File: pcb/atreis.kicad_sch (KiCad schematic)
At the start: 114 parts, among them SW1 SW_Push, U1 Elite-C

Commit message: Completed tracks and edge. Cleaned up drawings.
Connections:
- net ROW5: now also U1.17 (A0/PF7); no longer U1.13 (10/PB6)
- net ROW6: now also U1.16 (15/PB1); no longer U1.14 (16/PB2)
- net ROW8: now also U1.14 (16/PB2); no longer U1.16 (15/PB1)
- net ROW9: now also U1.13 (10/PB6); no longer U1.17 (A0/PF7)
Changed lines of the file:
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@@
     )
   )
-  (global_label "ROW5" (shape input) (at 111.76 170.18 0) (fields_autoplaced)
+  (global_label "ROW5" (shape input) (at 111.76 160.02 0) (fields_autoplaced)
     (effects (font (size 1.27 1.27)) (justify left))
-    (property "Intersheet References" "${INTERSHEET_REFS}" (id 0) (at -57.15 3.81 0)
+    (property "Intersheet References" "${INTERSHEET_REFS}" (id 0) (at -57.15 -6.35 0)
       (effects (font (size 1.27 1.27)) hide)
     )
@@
     )
   )
-  (global_label "ROW8" (shape input) (at 111.76 162.56 0) (fields_autoplaced)
+  (global_label "ROW8" (shape input) (at 111.76 167.64 0) (fields_autoplaced)
     (effects (font (size 1.27 1.27)) (justify left))
-    (property "Intersheet References" "${INTERSHEET_REFS}" (id 0) (at -57.15 -11.43 0)
+    (property "Intersheet References" "${INTERSHEET_REFS}" (id 0) (at -57.15 -6.35 0)
       (effects (font (size 1.27 1.27)) hide)
     )
@@
     )
   )
-  (global_label "ROW9" (shape input) (at 111.76 160.02 0) (fields_autoplaced)
+  (global_label "ROW9" (shape input) (at 111.76 170.18 0) (fields_autoplaced)
     (effects (font (size 1.27 1.27)) (justify left))
-    (property "Intersheet References" "${INTERSHEET_REFS}" (id 0) (at -57.15 -16.51 0)
+    (property "Intersheet References" "${INTERSHEET_REFS}" (id 0) (at -57.15 -6.35 0)
       (effects (font (size 1.27 1.27)) hide)
     )
@@
     )
   )
-  (global_label "ROW6" (shape input) (at 111.76 167.64 0) (fields_autoplaced)
+  (global_label "ROW6" (shape input) (at 111.76 162.56 0) (fields_autoplaced)
     (effects (font (size 1.27 1.27)) (justify left))
-    (property "Intersheet References" "${INTERSHEET_REFS}" (id 0) (at -57.15 -1.27 0)
+    (property "Intersheet References" "${INTERSHEET_REFS}" (id 0) (at -57.15 -6.35 0)
       (effects (font (size 1.27 1.27)) hide)
     )

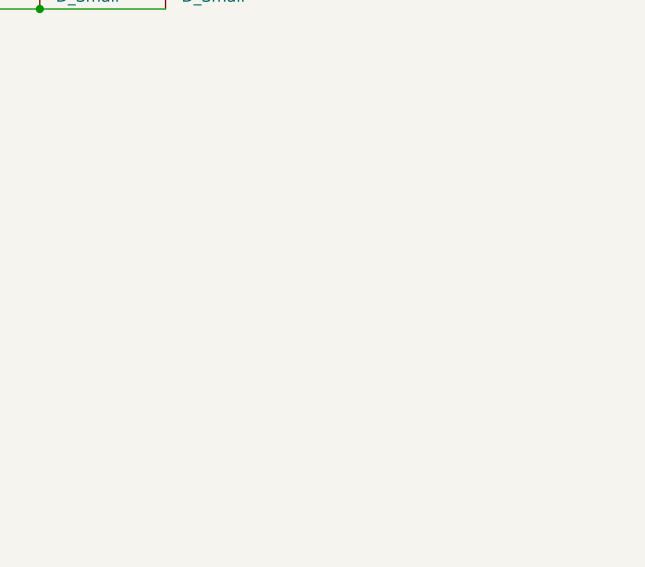
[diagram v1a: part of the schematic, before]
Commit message: Rerouted some of the tracks. Much nicer now. Rerouted tracks to make the holes thru holes, to use with spacers. Re-generated gerber file.
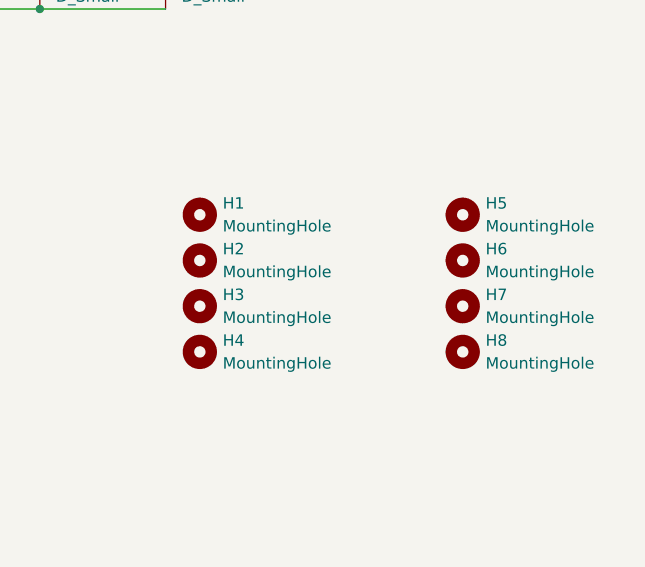
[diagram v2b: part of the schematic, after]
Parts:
- added H1, H2, H3, H4, H5, H6, H7, H8: MountingHole, kbd:M2_Hole_TH_Outside, symbol Mechanical:MountingHole
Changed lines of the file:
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@@
     (pin "2")
+  )
+  (symbol (lib_id "Mechanical:MountingHole") (at 175.26 144.78 0) (unit 1)
+    (in_bom yes) (on_board yes) (fields_autoplaced)
+    (property "Reference" "H3" (id 0) (at 177.8 143.5099 0)
+      (effects (font (size 1.27 1.27)) (justify left))
+    )
+    (property "Value" "MountingHole" (id 1) (at 177.8 146.0499 0)
+      (effects (font (size 1.27 1.27)) (justify left))
+    )
+    (property "Footprint" "kbd:M2_Hole_TH_Outside" (id 2) (at 175.26 144.78 0)
+      (effects (font (size 1.27 1.27)) hide)
+    )
+    (property "Datasheet" "~" (id 3) (at 175.26 144.78 0)
+      (effects (font (size 1.27 1.27)) hide)
+    )
   )
   (symbol (lib_id "MX_Alps_Hybrid:MX-NoLED") (at 203.2 69.85 0) (unit 1)
@@
     (pin "1")
     (pin "2")
+  )
+  (symbol (lib_id "Mechanical:MountingHole") (at 204.47 134.62 0) (unit 1)
+    (in_bom yes) (on_board yes) (fields_autoplaced)
+    (property "Reference" "H5" (id 0) (at 207.01 133.3499 0)
+      (effects (font (size 1.27 1.27)) (justify left))
+    )
+    (property "Value" "MountingHole" (id 1) (at 207.01 135.8899 0)
+      (effects (font (size 1.27 1.27)) (justify left))
+    )
+    (property "Footprint" "kbd:M2_Hole_TH_Outside" (id 2) (at 204.47 134.62 0)
+      (effects (font (size 1.27 1.27)) hide)
+    )
+    (property "Datasheet" "~" (id 3) (at 204.47 134.62 0)
+      (effects (font (size 1.27 1.27)) hide)
+    )
   )
   (symbol (lib_id "MX_Alps_Hybrid:MX-NoLED") (at 203.2 53.34 0) (unit 1)
@@
     (pin "9")
   )
+  (symbol (lib_id "Mechanical:MountingHole") (at 204.47 149.86 0) (unit 1)
+    (in_bom yes) (on_board yes) (fields_autoplaced)
+    (property "Reference" "H8" (id 0) (at 207.01 148.5899 0)
+      (effects (font (size 1.27 1.27)) (justify left))
+    )
+    (property "Value" "MountingHole" (id 1) (at 207.01 151.1299 0)
+      (effects (font (size 1.27 1.27)) (justify left))
+    )
+    (property "Footprint" "kbd:M2_Hole_TH_Outside" (id 2) (at 204.47 149.86 0)
+      (effects (font (size 1.27 1.27)) hide)
+    )
+    (property "Datasheet" "~" (id 3) (at 204.47 149.86 0)
+      (effects (font (size 1.27 1.27)) hide)
+    )
+  )
   (symbol (lib_id "Device:D_Small") (at 185.42 92.71 90) (unit 1)
     (in_bom yes) (on_board yes)
@@
     (pin "1")
     (pin "2")
+  )
+  (symbol (lib_id "Mechanical:MountingHole") (at 175.26 149.86 0) (unit 1)
+    (in_bom yes) (on_board yes) (fields_autoplaced)
+    (property "Reference" "H4" (id 0) (at 177.8 148.5899 0)
+      (effects (font (size 1.27 1.27)) (justify left))
+    )
+    (property "Value" "MountingHole" (id 1) (at 177.8 151.1299 0)
+      (effects (font (size 1.27 1.27)) (justify left))
+    )
+    (property "Footprint" "kbd:M2_Hole_TH_Outside" (id 2) (at 175.26 149.86 0)
+      (effects (font (size 1.27 1.27)) hide)
+    )
+    (property "Datasheet" "~" (id 3) (at 175.26 149.86 0)
+      (effects (font (size 1.27 1.27)) hide)
+    )
   )
   (symbol (lib_id "MX_Alps_Hybrid:MX-NoLED") (at 147.32 69.85 0) (unit 1)
@@
     (pin "2")
   )
+  (symbol (lib_id "Mechanical:MountingHole") (at 204.47 139.7 0) (unit 1)
+    (in_bom yes) (on_board yes) (fields_autoplaced)
+    (property "Reference" "H6" (id 0) (at 207.01 138.4299 0)
+      (effects (font (size 1.27 1.27)) (justify left))
+    )
+    (property "Value" "MountingHole" (id 1) (at 207.01 140.9699 0)
+      (effects (font (size 1.27 1.27)) (justify left))
+    )
+    (property "Footprint" "kbd:M2_Hole_TH_Outside" (id 2) (at 204.47 139.7 0)
+      (effects (font (size 1.27 1.27)) hide)
+    )
+    (property "Datasheet" "~" (id 3) (at 204.47 139.7 0)
+      (effects (font (size 1.27 1.27)) hide)
+    )
+  )
   (symbol (lib_id "Device:D_Small") (at 35.56 59.69 90) (unit 1)
     (in_bom yes) (on_board yes)
@@
     (pin "2")
   )
+  (symbol (lib_id "Mechanical:MountingHole") (at 175.26 134.62 0) (unit 1)
+    (in_bom yes) (on_board yes) (fields_autoplaced)
+    (property "Reference" "H1" (id 0) (at 177.8 133.3499 0)
+      (effects (font (size 1.27 1.27)) (justify left))
+    )
+    (property "Value" "MountingHole" (id 1) (at 177.8 135.8899 0)
+      (effects (font (size 1.27 1.27)) (justify left))
+    )
+    (property "Footprint" "kbd:M2_Hole_TH_Outside" (id 2) (at 175.26 134.62 0)
+      (effects (font (size 1.27 1.27)) hide)
+    )
+    (property "Datasheet" "~" (id 3) (at 175.26 134.62 0)
+      (effects (font (size 1.27 1.27)) hide)
+    )
+  )
   (symbol (lib_id "MX_Alps_Hybrid:MX-NoLED") (at 189.23 36.83 0) (unit 1)
     (in_bom yes) (on_board yes)
@@
     (pin "2")
   )
+  (symbol (lib_id "Mechanical:MountingHole") (at 204.47 144.78 0) (unit 1)
+    (in_bom yes) (on_board yes) (fields_autoplaced)
+    (property "Reference" "H7" (id 0) (at 207.01 143.5099 0)
+      (effects (font (size 1.27 1.27)) (justify left))
+    )
+    (property "Value" "MountingHole" (id 1) (at 207.01 146.0499 0)
+      (effects (font (size 1.27 1.27)) (justify left))
+    )
+    (property "Footprint" "kbd:M2_Hole_TH_Outside" (id 2) (at 204.47 144.78 0)
+      (effects (font (size 1.27 1.27)) hide)
+    )
+    (property "Datasheet" "~" (id 3) (at 204.47 144.78 0)
+      (effects (font (size 1.27 1.27)) hide)
+    )
+  )
   (symbol (lib_id "MX_Alps_Hybrid:MX-NoLED") (at 95.25 69.85 0) (unit 1)
     (in_bom yes) (on_board yes)
@@
     (pin "1")
     (pin "2")
+  )
+  (symbol (lib_id "Mechanical:MountingHole") (at 175.26 139.7 0) (unit 1)
+    (in_bom yes) (on_board yes) (fields_autoplaced)
+    (property "Reference" "H2" (id 0) (at 177.8 138.4299 0)
+      (effects (font (size 1.27 1.27)) (justify left))
+    )
+    (property "Value" "MountingHole" (id 1) (at 177.8 140.9699 0)
+      (effects (font (size 1.27 1.27)) (justify left))
+    )
+    (property "Footprint" "kbd:M2_Hole_TH_Outside" (id 2) (at 175.26 139.7 0)
+      (effects (font (size 1.27 1.27)) hide)
+    )
+    (property "Datasheet" "~" (id 3) (at 175.26 139.7 0)
+      (effects (font (size 1.27 1.27)) hide)
+    )
   )
   (symbol (lib_id "Device:D_Small") (at 171.45 59.69 90) (unit 1)
@@
       (reference "D56") (unit 1) (value "D_Small") (footprint "atreis:D3_hybrid_common_hole")
     )
+    (path "/a24665dd-f547-4b22-bca9-e623facf4851"
+      (reference "H1") (unit 1) (value "MountingHole") (footprint "kbd:M2_Hole_TH_Outside")
+    )
+    (path "/ade271db-05bf-4376-8f80-56d1f37eb279"
+      (reference "H2") (unit 1) (value "MountingHole") (footprint "kbd:M2_Hole_TH_Outside")
+    )
+    (path "/2e74c5cf-df21-4ecb-90c2-e2781152c95b"
+      (reference "H3") (unit 1) (value "MountingHole") (footprint "kbd:M2_Hole_TH_Outside")
+    )
+    (path "/6fdc6513-85fa-4ac4-9fba-94c952fa0cb6"
+      (reference "H4") (unit 1) (value "MountingHole") (footprint "kbd:M2_Hole_TH_Outside")
+    )
+    (path "/3c366a71-f7c8-4705-a28c-1a6b708315a6"
+      (reference "H5") (unit 1) (value "MountingHole") (footprint "kbd:M2_Hole_TH_Outside")
+    )
+    (path "/9c917ee8-79d7-48ac-bc50-06e14fe92704"
+      (reference "H6") (unit 1) (value "MountingHole") (footprint "kbd:M2_Hole_TH_Outside")
+    )
+    (path "/a893fab4-93c7-43da-a20e-5bc79508e66b"
+      (reference "H7") (unit 1) (value "MountingHole") (footprint "kbd:M2_Hole_TH_Outside")
+    )
+    (path "/5806f166-c5b7-446b-9db4-5eae522d94cc"
+      (reference "H8") (unit 1) (value "MountingHole") (footprint "kbd:M2_Hole_TH_Outside")
+    )
     (path "/2e28c491-81a5-4ab7-b965-ecc1711bc95e"
